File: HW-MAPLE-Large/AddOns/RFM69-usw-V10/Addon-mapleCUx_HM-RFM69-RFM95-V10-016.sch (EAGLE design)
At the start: 35 parts, among them IC1 ATSHA204A, IC31 ATMEGA168-TQFP, X31 M03X2, X4 1751248, X7 1751264, Y2 8MHZ

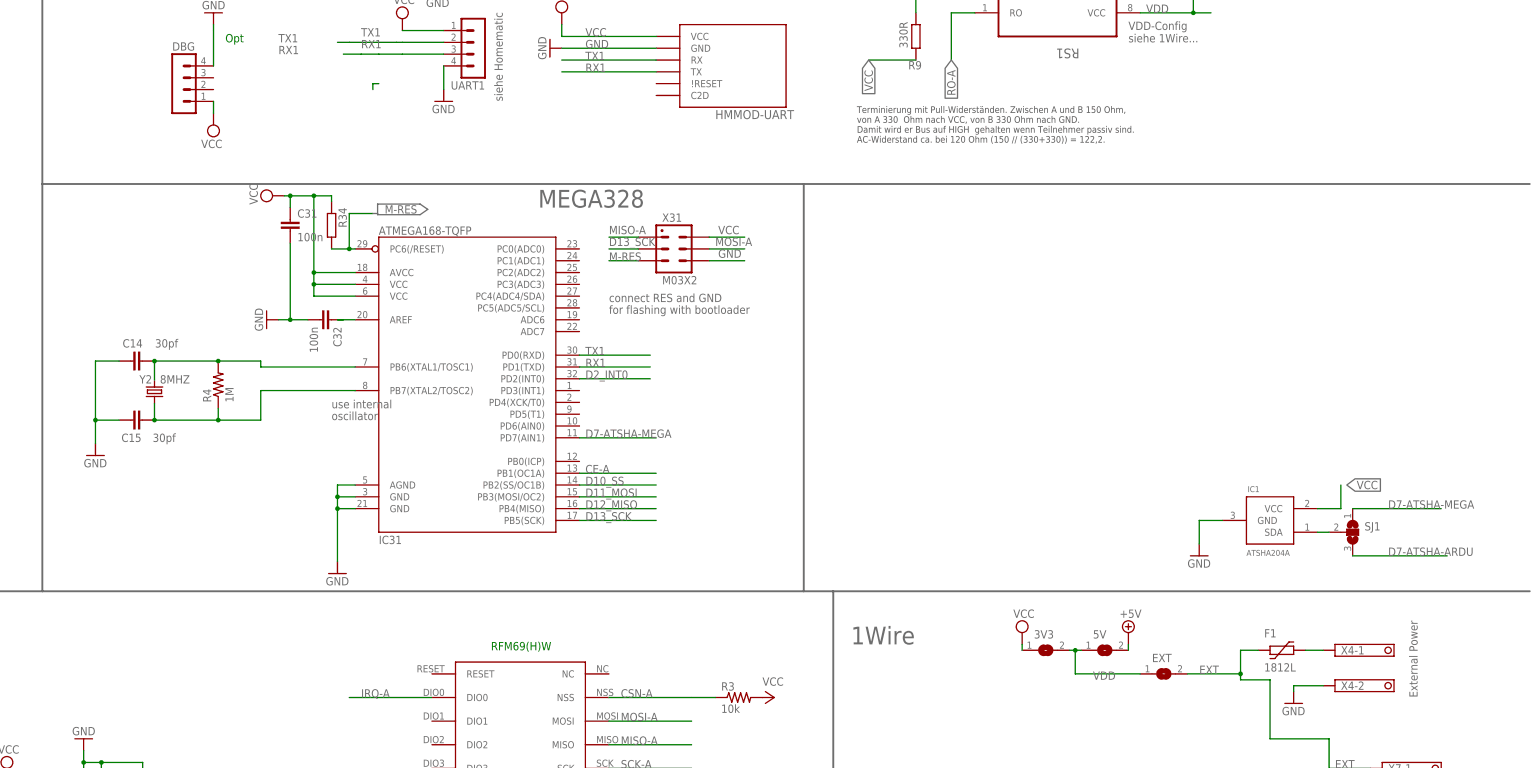
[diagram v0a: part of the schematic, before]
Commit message: Addon: plus RFM95
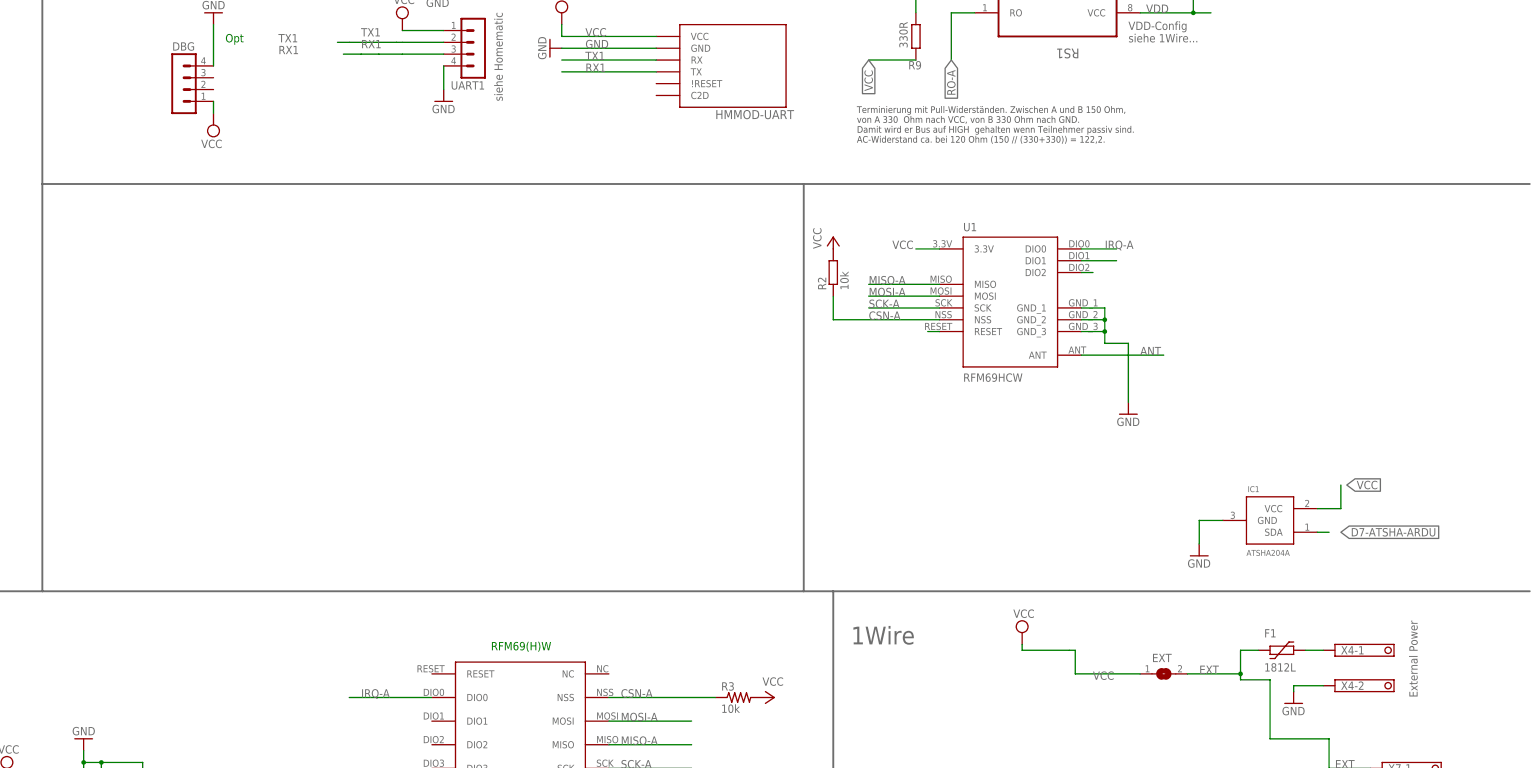
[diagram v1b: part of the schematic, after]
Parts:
- removed 3V3, 5V: (no value), jumper:SJ
- removed C14, C15: 30pf, doug:CAP0805
- removed C31, C32: 100n, rcl:C-EUC0805
- removed IC31: ATMEGA168-TQFP, atmel:ATMEGA168-TQFP
- removed R34: (no value), rcl:R-EU_R0805
- removed R4: 1M, doug:RESISTOR0805-RES
- removed SJ1: (no value), jumper:SJ2W
- removed X31: M03X2, mechanics:M03X2
- removed Y2: 8MHZ, SparkFun-FreqCtrl:CRYSTALTXC-7A
- added R2: 10k, rcl:R-EU_M0805
- added U1: RFM69HCW, doug:RFM69HCW
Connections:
- removed net +5V: 5V.2
- removed net D10_SS: IC31.PB2(SS/OC1B)
- removed net D11_MOSI: IC31.PB3(MOSI/OC2)
- removed net D12_MISO: IC31.PB4(MISO)
- removed net D13_SCK: IC31.PB5(SCK), X31.3
- removed net D2_INT0: IC31.PD2(INT0)
- removed net D7-ATSHA-MEGA: IC31.PD7(AIN1), SJ1.1
- removed net M-RES: IC31.PC6(/RESET), R34.2, X31.5
- removed net N$1: ANT1.1, RFM69W.ANT, X2.ANT
- removed net N$13: C32.1, IC31.AREF
- removed net N$19: C15.2, IC31.PB7(XTAL2/TOSC2), R4.1, Y2.1
- removed net N$3: C14.2, IC31.PB6(XTAL1/TOSC1), R4.2, Y2.2
- removed net N$5: IC1.SDA, SJ1.2
- new net ANT: ANT1.1, RFM69W.ANT, U1.ANT, X2.ANT
- new net N$14: U1.DIO2
- new net N$15: U1.DIO1
- new net N$2: U1.RESET
- net CE-A: no longer IC31.PB1(OC1A)
- net CSN-A: now also R2.1, U1.NSS
- net D7-ATSHA-ARDU: now also IC1.SDA; no longer SJ1.3
- net GND: now also U1.GND_1, U1.GND_2, U1.GND_3; no longer C14.1, C15.1, C31.2, C32.2, IC31.AGND, IC31.GND@1, IC31.GND@2, X31.6
- net IRQ-A: now also U1.DIO0
- net MISO-A: now also U1.MISO; no longer X31.1
- net MOSI-A: now also U1.MOSI; no longer X31.4
- net RX1: no longer IC31.PD1(TXD)
- net SCK-A: now also U1.SCK
- net TX1: no longer IC31.PD0(RXD)
- net VCC: now also EXT.1, R2.2, U1.3.3V; no longer 3V3.1, C31.1, IC31.AVCC, IC31.VCC@1, IC31.VCC@2, R34.1, X31.2
- net VDD: no longer 3V3.2, 5V.1, EXT.1
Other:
- note removed: "MEGA328"
- note removed: "connect RES and GND"
- note removed: "for flashing with bootloader"
- note removed: "oscillator"
- note removed: "use internal"
